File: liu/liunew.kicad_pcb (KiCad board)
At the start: 2 copper layers, 96.5 x 66 mm, 20 parts, among them J1 Screw Termial, J2 Screw Terminal, J3 Screw Termial, J4 Screw Termial, J5 I2C, J6 RotaryEncoder, U1 VoltageRegulator, U2 ESP32, U3 TJA1050

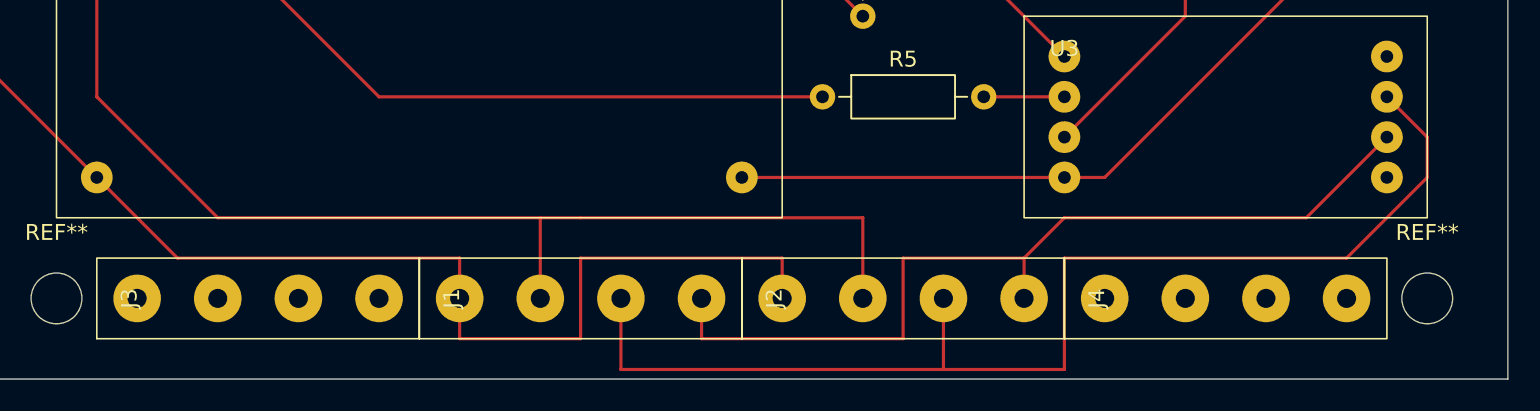
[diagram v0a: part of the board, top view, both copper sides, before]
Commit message: 4 screw terminals
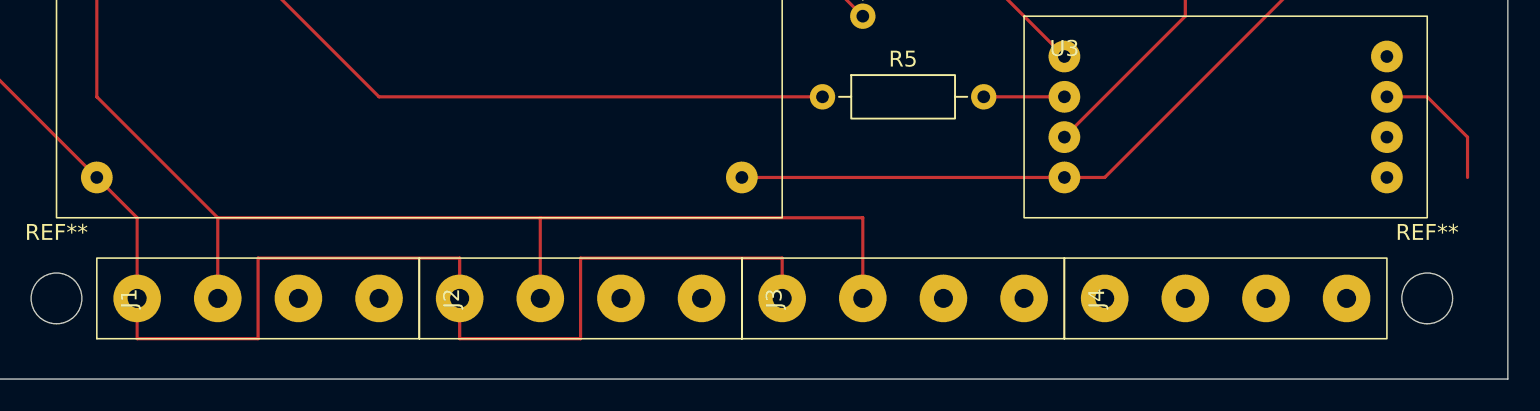
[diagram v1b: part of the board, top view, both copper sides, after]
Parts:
- moved J3 40.6 mm to (76.2, 86.4)
- moved J1 20.3 mm to (35.6, 86.4)
- moved J2 20.3 mm to (55.9, 86.4)
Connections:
- J3 pad 1: unconnected-(J3-Pin_1-Pad1) -> /GND
- J3 pad 2: unconnected-(J3-Pin_2-Pad2) -> /12V
- J3 pad 3: unconnected-(J3-Pin_3-Pad3) -> /CANH
- J3 pad 4: unconnected-(J3-Pin_4-Pad4) -> /CANL
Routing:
- net /CANH: track 75.0 -> 8.67 mm
- net /CANL: track 56.5 -> 0.00 mm
- net /GND: track 245.2 -> 256.8 mm
- net /12V: track 74.3 -> 79.4 mm
